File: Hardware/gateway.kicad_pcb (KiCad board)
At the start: 2 copper layers, 65 x 56 mm, 27 parts, among them J0 Raspberry_Pi_2_3_40HAT, J1 CONN_01X02, J2 Conn_Coaxial, J3 Conn_Coaxial, U0 CAT24C32, U0a1 DRF1278F, U0b1 XL1278-SMT, U0c1 RFM9xW-xxxS2, U1a1 DRF1278F, U1b1 XL1278-SMT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

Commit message: Adjust footprints and add vias as per #1 Updated XL1278-SMT and DRF1278F footprints from matburnham/kicad-libs#1. Changed SMA footprint. Added some more GND vias.
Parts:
- J2, J3: footprint Connector_Coaxial:SMA_Molex_73251-1153_EdgeMount_Horizontal -> Connector_Coaxial:SMA_Samtec_SMA-J-P-X-ST-EM1_EdgeMount
- moved U0a1 4.80 mm to (117.6, 88.3)
- moved U1a1 4.79 mm to (117.6, 113.7)
- moved U0b1 4.66 mm to (111.9, 88.3)
- moved U1b1 4.58 mm to (111.8, 113.7)
- moved J3 2.54 mm to (80.6, 103.8), turned to 270 degrees
- moved J2 2.36 mm to (80.6, 73.7), turned to 270 degrees
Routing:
- net GND: track 97.4 -> 108.0 mm, vias 92 -> 133
- net 1_DIO5: track 64.7 -> 67.4 mm
- net 0_DIO5: track 43.0 -> 44.7 mm
- net VCC: track 157.1 -> 158.1 mm
- net 1_DIO0: track 112.6 -> 113.6 mm
- net 0_ANT: track 35.5 -> 36.3 mm
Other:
- board text added: "Raspberry Pi LoRa expansion board v1.1 - MBB"
- board text added: "Raspberry Pi LoRa expansion board v1.1 2021-05 MBB"
- board text removed: "Raspberry Pi LoRa expansion board v1.0 - MBB"
- board text removed: "Raspberry Pi LoRa expansion board v1.0 2021-03 MBB"

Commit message: Tweaks for #1.
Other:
- board text added: "Raspberry Pi LoRa expansion board v1.1 2021-05 MBB git.io/Jm1XT"
- board text removed: "Raspberry Pi LoRa expansion board v1.1 - MBB"
- board text removed: "Raspberry Pi LoRa expansion board v1.1 2021-05 MBB"

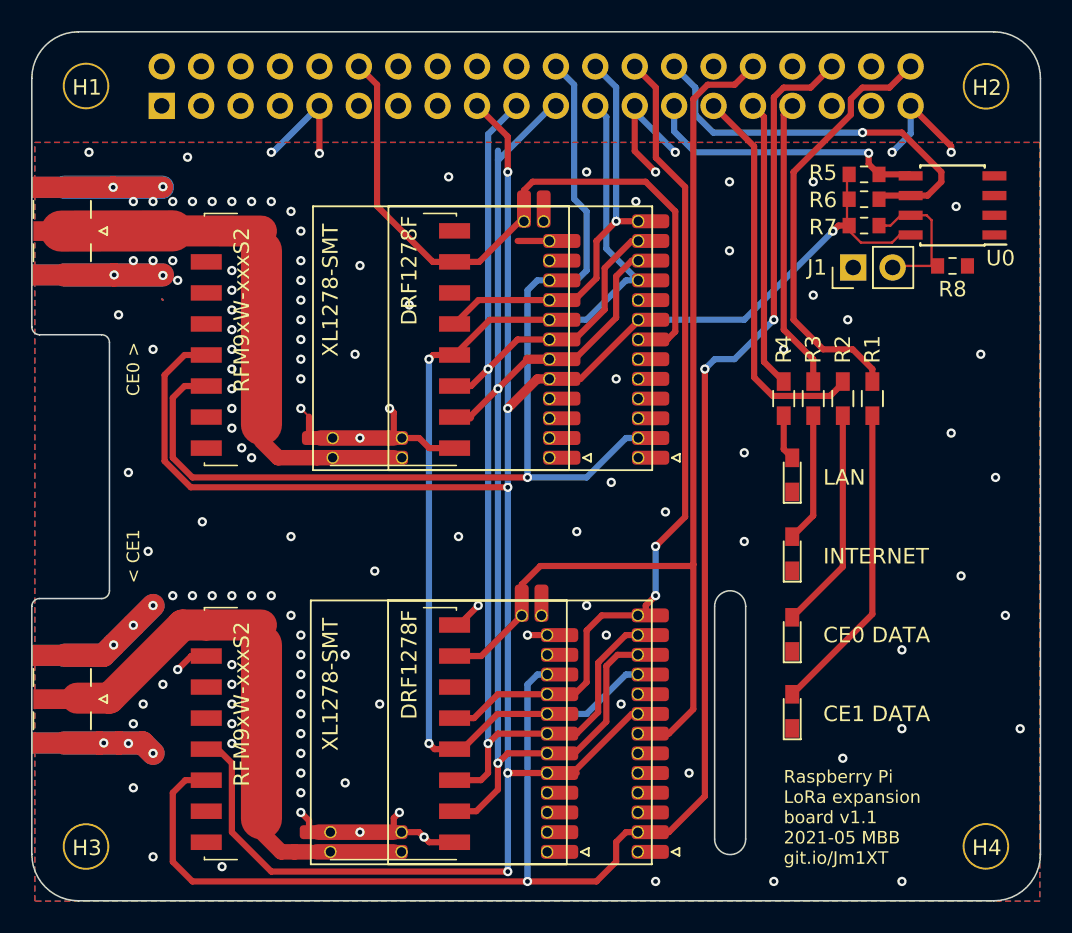
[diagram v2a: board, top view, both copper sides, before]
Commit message: Fix #2 Adds a breakout for CE0, but not for CE1 as there's insufficient space.
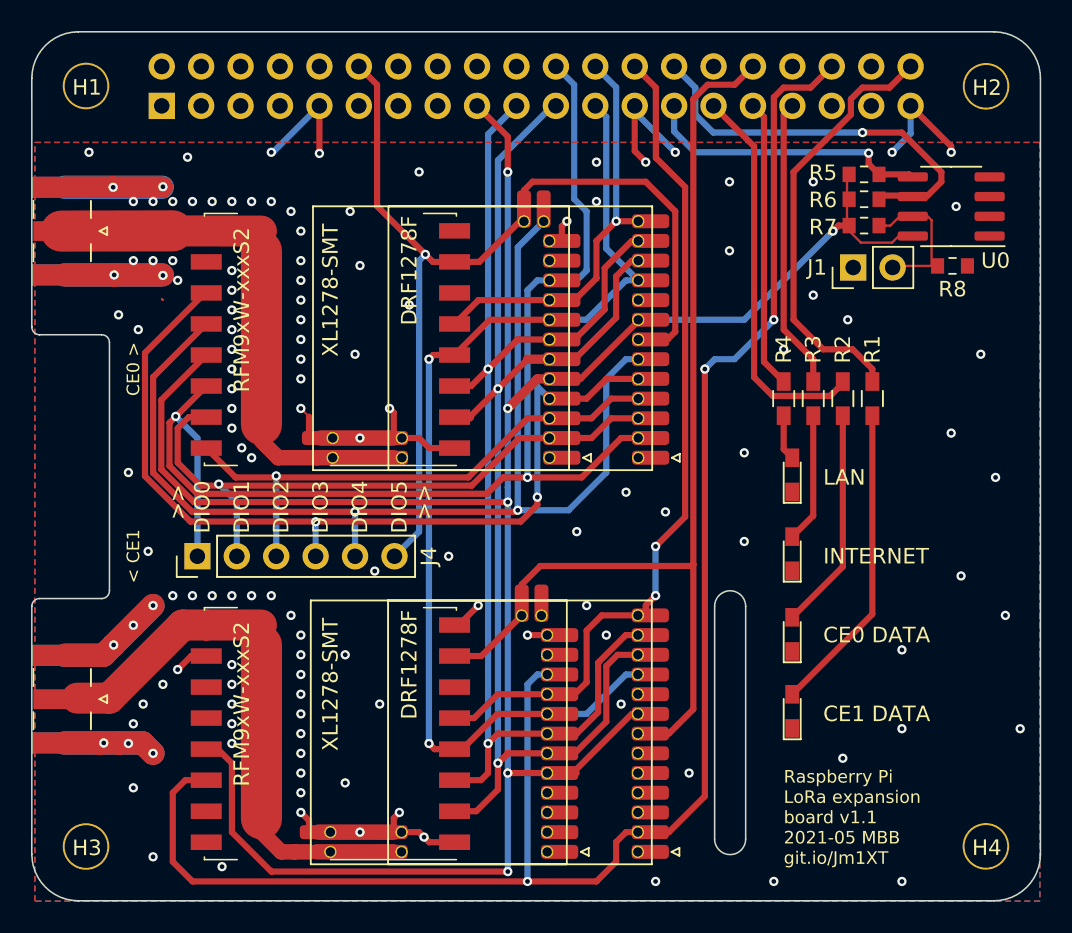
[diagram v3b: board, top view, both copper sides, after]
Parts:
- added J4: Conn_01x06, Connector_PinHeader_2.54mm:PinHeader_1x06_P2.54mm_Vertical, F.Cu at (89.2, 94.6)
- U0: footprint Package_SOIC:SOIC-8_3.9x4.9mm_P1.27mm -> Package_SO:SOIC-8_3.9x4.9mm_P1.27mm
- moved U0 0.11 mm to (137.8, 72.1)
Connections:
- U0a1 pad 3: Net-(U0a1-Pad3) -> 0_DIO1
- U0a1 pad 4: Net-(U0a1-Pad4) -> 0_DIO2
- U0a1 pad 5: Net-(U0a1-Pad5) -> 0_DIO3
- U0a1 pad 6: Net-(U0a1-Pad6) -> 0_DIO4
- U0b1 pad 13: Net-(U0b1-Pad13) -> 0_DIO4
- U0b1 pad 2: Net-(U0b1-Pad2) -> 0_DIO1
- U0b1 pad 3: Net-(U0b1-Pad3) -> 0_DIO2
- U0b1 pad 4: Net-(U0b1-Pad4) -> 0_DIO3
- U0c1 pad 11: (no net) -> 0_DIO3
- U0c1 pad 12: (no net) -> 0_DIO4
- U0c1 pad 15: (no net) -> 0_DIO1
- U0c1 pad 16: (no net) -> 0_DIO2
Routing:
- net 0_DIO4: track 0.00 -> 73.0 mm, vias 0 -> 2
- net 0_DIO3: track 0.00 -> 57.6 mm, vias 0 -> 2
- net 0_DIO1: track 0.00 -> 44.5 mm, vias 0 -> 1
- net 0_DIO2: track 0.00 -> 36.7 mm, vias 0 -> 1
- net 0_DIO5: track 44.7 -> 65.0 mm, vias 0 -> 1
- net 0_DIO0: track 68.3 -> 79.3 mm, vias 1 -> 2
- net GND: track 108.0 -> 106.2 mm, vias 133 -> 132
- net MISO: track 85.5 -> 84.9 mm
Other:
- board text added: ">>"
- board text added: "DIO0"
- board text added: "DIO1"
- board text added: "DIO2"
- board text added: "DIO3"
- board text added: "DIO4"
- board text added: "DIO5"
